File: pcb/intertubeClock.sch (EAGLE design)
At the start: 89 parts, among them Q1 BSA223SP, Q10 BSA223SP, Q11 BSA223SP, Q12 BSA223SP, Q13 BSA223SP, Q14 BSA223SP, Q15 BSA223SP, Q16 BSA223SP, Q2 BSA223SP, Q3 BSA223SP, Q4 BSA223SP, Q5 BSA223SP, Q6 BSA223SP, Q7 BSA223SP, Q8 BSA223SP, Q9 BSA223SP, U1 HV5122PG, U2 HV5122PG

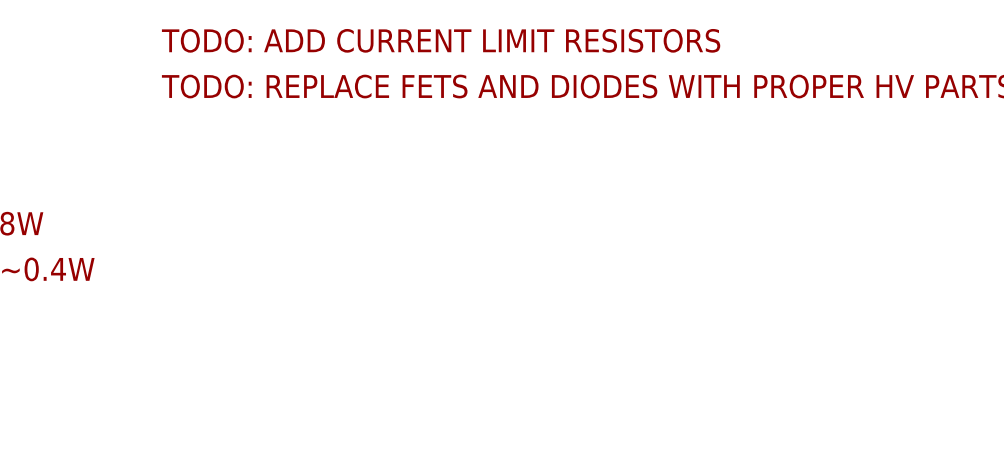
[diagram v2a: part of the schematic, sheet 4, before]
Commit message: -Fixed voltage divider values. -Added diodes.
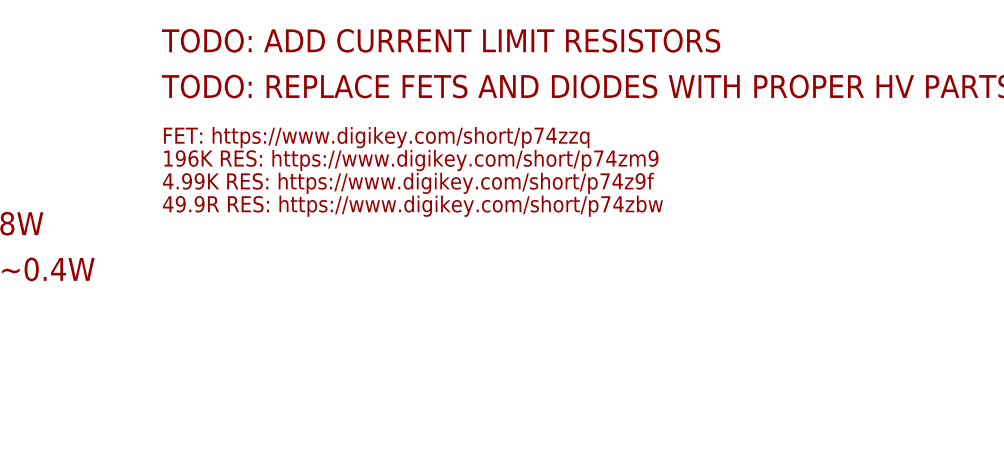
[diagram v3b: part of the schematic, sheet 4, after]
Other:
- note added: "196K RES: https://www.digikey.com/short/p74zm9"
- note added: "4.99K RES: https://www.digikey.com/short/p74z9f"
- note added: "49.9R RES: https://www.digikey.com/short/p74zbw"
- note added: "FET: https://www.digikey.com/short/p74zzq"
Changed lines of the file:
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@@
 <grid distance="0.1" unitdist="inch" unit="inch" style="lines" multiple="1" display="no" altdistance="0.01" altunitdist="inch" altunit="inch"/>
 <layers>
-<layer number="1" name="Top" color="4" fill="1" visible="yes" active="no"/>
-<layer number="2" name="Route2" color="1" fill="3" visible="yes" active="no"/>
-<layer number="3" name="Route3" color="4" fill="3" visible="yes" active="no"/>
-<layer number="4" name="Route4" color="1" fill="4" visible="yes" active="no"/>
-<layer number="5" name="Route5" color="4" fill="4" visible="yes" active="no"/>
-<layer number="6" name="Route6" color="1" fill="8" visible="yes" active="no"/>
-<layer number="7" name="Route7" color="4" fill="8" visible="yes" active="no"/>
-<layer number="8" name="Route8" color="1" fill="2" visible="yes" active="no"/>
-<layer number="9" name="Route9" color="4" fill="2" visible="yes" active="no"/>
-<layer number="10" name="Route10" color="1" fill="7" visible="yes" active="no"/>
-<layer number="11" name="Route11" color="4" fill="7" visible="yes" active="no"/>
-<layer number="12" name="Route12" color="1" fill="5" visible="yes" active="no"/>
-<layer number="13" name="Route13" color="4" fill="5" visible="yes" active="no"/>
-<layer number="14" name="Route14" color="1" fill="6" visible="yes" active="no"/>
-<layer number="15" name="Route15" color="4" fill="6" visible="yes" active="no"/>
-<layer number="16" name="Bottom" color="1" fill="1" visible="yes" active="no"/>
-<layer number="17" name="Pads" color="2" fill="1" visible="yes" active="no"/>
-<layer number="18" name="Vias" color="2" fill="1" visible="yes" active="no"/>
-<layer number="19" name="Unrouted" color="6" fill="1" visible="yes" active="no"/>
-<layer number="20" name="Dimension" color="15" fill="1" visible="yes" active="no"/>
-<layer number="21" name="tPlace" color="7" fill="1" visible="yes" active="no"/>
-<layer number="22" name="bPlace" color="7" fill="1" visible="yes" active="no"/>
-<layer number="23" name="tOrigins" color="15" fill="1" visible="yes" active="no"/>
-<layer number="24" name="bOrigins" color="15" fill="1" visible="yes" active="no"/>
-<layer number="25" name="tNames" color="7" fill="1" visible="yes" active="no"/>
-<layer number="26" name="bNames" color="7" fill="1" visible="yes" active="no"/>
-<layer number="27" name="tValues" color="7" fill="1" visible="yes" active="no"/>
-<layer number="28" name="bValues" color="7" fill="1" visible="yes" active="no"/>
+<layer number="1" name="Top" color="4" fill="1" visible="no" active="no"/>
+<layer number="2" name="Route2" color="1" fill="3" visible="no" active="no"/>
+<layer number="3" name="Route3" color="4" fill="3" visible="no" active="no"/>
+<layer number="4" name="Route4" color="1" fill="4" visible="no" active="no"/>
+<layer number="5" name="Route5" color="4" fill="4" visible="no" active="no"/>
+<layer number="6" name="Route6" color="1" fill="8" visible="no" active="no"/>
+<layer number="7" name="Route7" color="4" fill="8" visible="no" active="no"/>
+<layer number="8" name="Route8" color="1" fill="2" visible="no" active="no"/>
+<layer number="9" name="Route9" color="4" fill="2" visible="no" active="no"/>
+<layer number="10" name="Route10" color="1" fill="7" visible="no" active="no"/>
+<layer number="11" name="Route11" color="4" fill="7" visible="no" active="no"/>
+<layer number="12" name="Route12" color="1" fill="5" visible="no" active="no"/>
+<layer number="13" name="Route13" color="4" fill="5" visible="no" active="no"/>
+<layer number="14" name="Route14" color="1" fill="6" visible="no" active="no"/>
+<layer number="15" name="Route15" color="4" fill="6" visible="no" active="no"/>
+<layer number="16" name="Bottom" color="1" fill="1" visible="no" active="no"/>
+<layer number="17" name="Pads" color="2" fill="1" visible="no" active="no"/>
+<layer number="18" name="Vias" color="2" fill="1" visible="no" active="no"/>
+<layer number="19" name="Unrouted" color="6" fill="1" visible="no" active="no"/>
+<layer number="20" name="Dimension" color="15" fill="1" visible="no" active="no"/>
+<layer number="21" name="tPlace" color="7" fill="1" visible="no" active="no"/>
+<layer number="22" name="bPlace" color="7" fill="1" visible="no" active="no"/>
+<layer number="23" name="tOrigins" color="15" fill="1" visible="no" active="no"/>
+<layer number="24" name="bOrigins" color="15" fill="1" visible="no" active="no"/>
+<layer number="25" name="tNames" color="7" fill="1" visible="no" active="no"/>
+<layer number="26" name="bNames" color="7" fill="1" visible="no" active="no"/>
+<layer number="27" name="tValues" color="7" fill="1" visible="no" active="no"/>
+<layer number="28" name="bValues" color="7" fill="1" visible="no" active="no"/>
 <layer number="29" name="tStop" color="7" fill="3" visible="no" active="no"/>
 <layer number="30" name="bStop" color="7" fill="6" visible="no" active="no"/>
@@
 <layer number="35" name="tGlue" color="7" fill="4" visible="no" active="no"/>
 <layer number="36" name="bGlue" color="7" fill="5" visible="no" active="no"/>
-<layer number="37" name="tTest" color="7" fill="1" visible="yes" active="no"/>
-<layer number="38" name="bTest" color="7" fill="1" visible="yes" active="no"/>
+<layer number="37" name="tTest" color="7" fill="1" visible="no" active="no"/>
+<layer number="38" name="bTest" color="7" fill="1" visible="no" active="no"/>
 <layer number="39" name="tKeepout" color="4" fill="11" visible="no" active="no"/>
 <layer number="40" name="bKeepout" color="1" fill="11" visible="no" active="no"/>
@@
 <layer number="44" name="Drills" color="7" fill="1" visible="no" active="no"/>
 <layer number="45" name="Holes" color="7" fill="1" visible="no" active="no"/>
-<layer number="46" name="Milling" color="3" fill="1" visible="yes" active="no"/>
-<layer number="47" name="Measures" color="7" fill="1" visible="yes" active="no"/>
-<layer number="48" name="Document" color="7" fill="1" visible="yes" active="no"/>
-<layer number="49" name="Reference" color="7" fill="1" visible="yes" active="no"/>
-<layer number="51" name="tDocu" color="7" fill="1" visible="yes" active="no"/>
-<layer number="52" name="bDocu" color="7" fill="1" visible="yes" active="no"/>
+<layer number="46" name="Milling" color="3" fill="1" visible="no" active="no"/>
+<layer number="47" name="Measures" color="7" fill="1" visible="no" active="no"/>
+<layer number="48" name="Document" color="7" fill="1" visible="no" active="no"/>
+<layer number="49" name="Reference" color="7" fill="1" visible="no" active="no"/>
+<layer number="51" name="tDocu" color="7" fill="1" visible="no" active="no"/>
+<layer number="52" name="bDocu" color="7" fill="1" visible="no" active="no"/>
 <layer number="90" name="Modules" color="5" fill="1" visible="yes" active="yes"/>
 <layer number="91" name="Nets" color="2" fill="1" visible="yes" active="yes"/>
@@
 <text x="27.94" y="238.76" size="2.54" layer="94">Vba limiter dissipation = ~0.8W</text>
 <text x="27.94" y="233.68" size="2.54" layer="94">Vba_off limiter dissipation = ~0.4W</text>
+<text x="91.44" y="248.92" size="1.778" layer="94">FET: https://www.digikey.com/short/p74zzq</text>
+<text x="91.44" y="246.38" size="1.778" layer="94">196K RES: https://www.digikey.com/short/p74zm9</text>
+<text x="91.44" y="243.84" size="1.778" layer="94">4.99K RES: https://www.digikey.com/short/p74z9f</text>
+<text x="91.44" y="241.3" size="1.778" layer="94">49.9R RES: https://www.digikey.com/short/p74zbw</text>
 </plain>
 <instances>

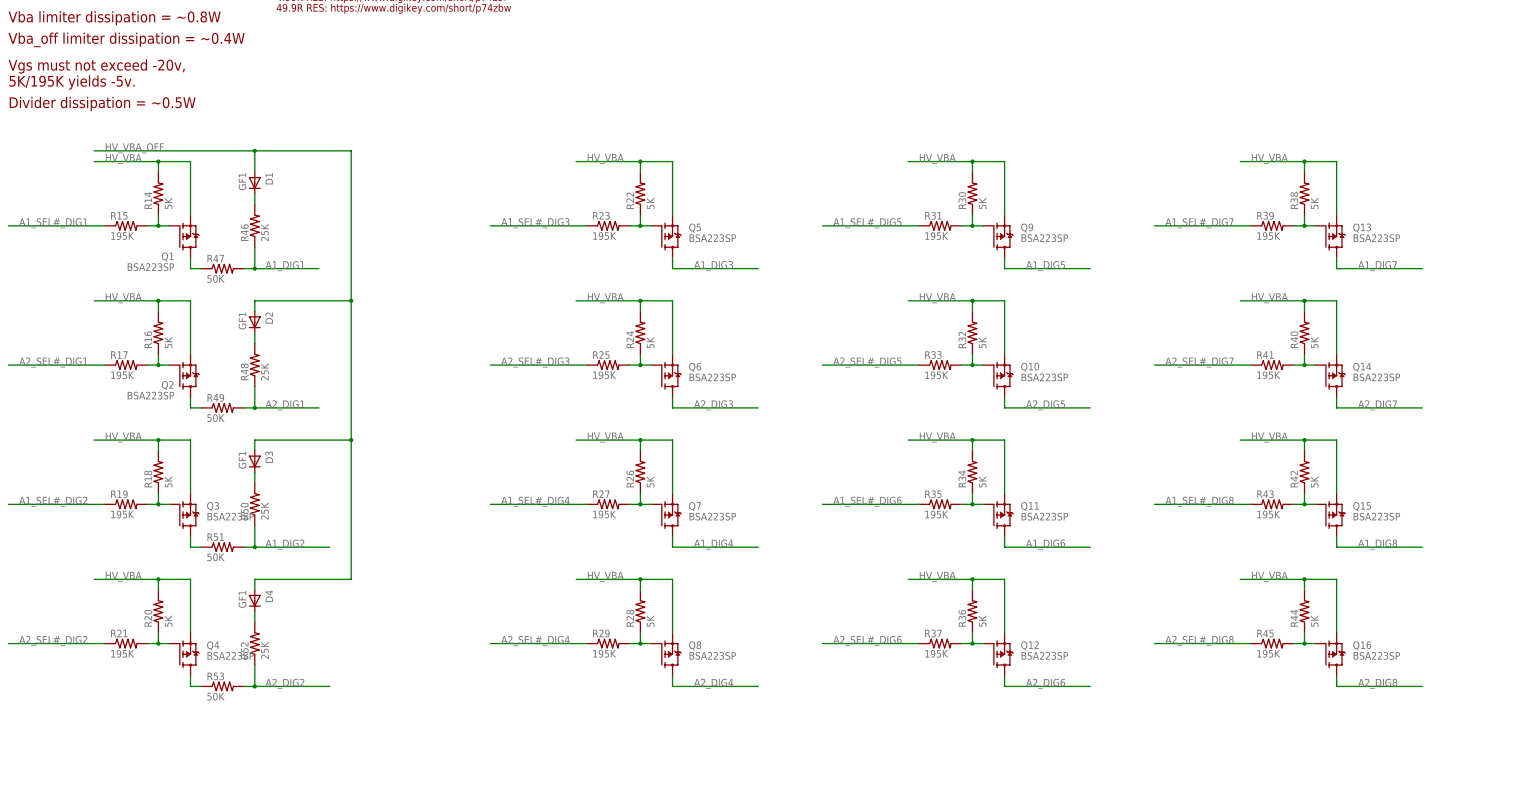
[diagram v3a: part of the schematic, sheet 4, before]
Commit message: -Added remaining components.
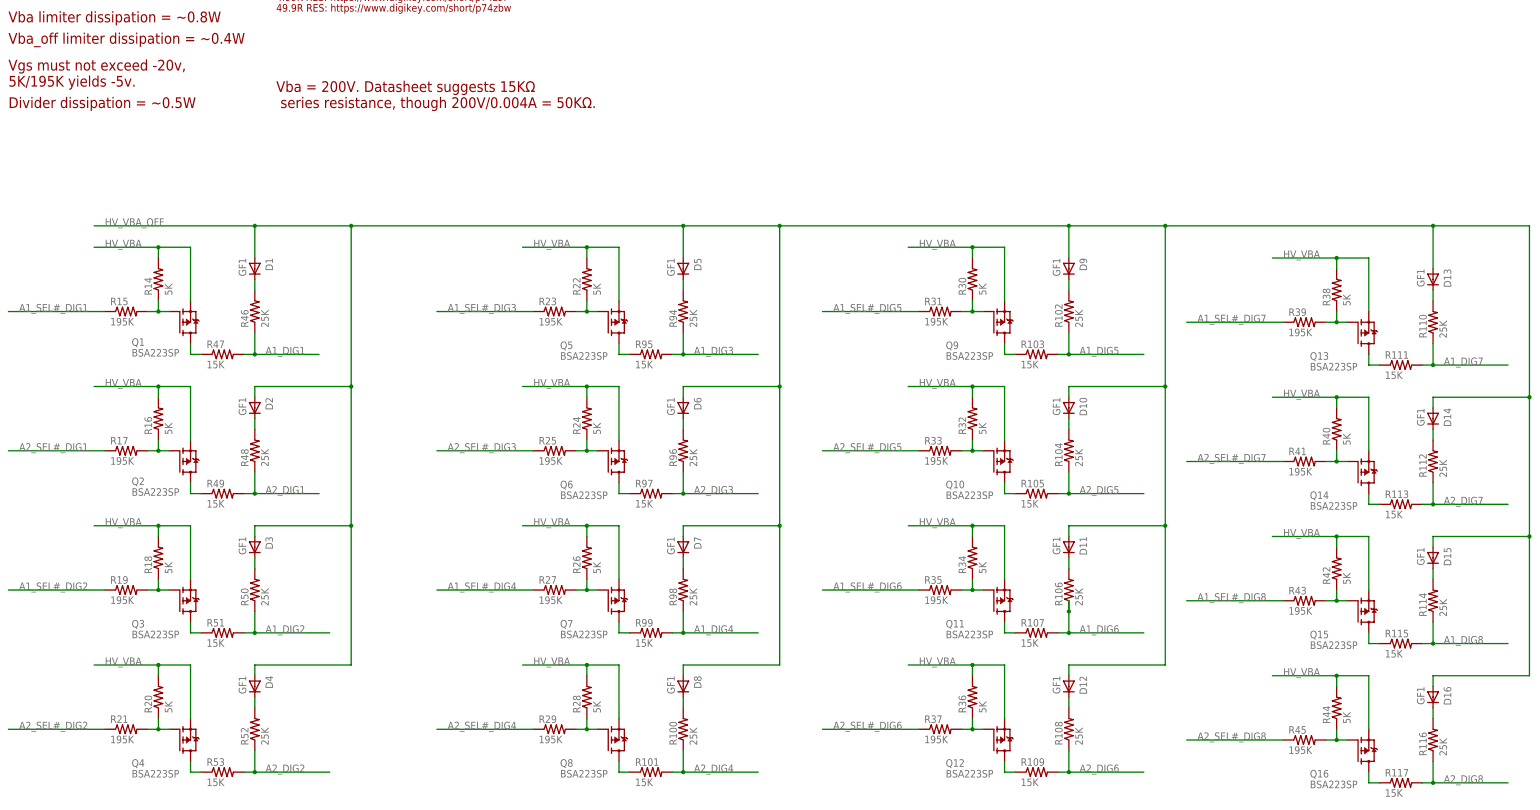
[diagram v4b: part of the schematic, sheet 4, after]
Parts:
- added D10, D11, D12, D13, D14, D15, D16, D5, D6, D7, D8, D9: GF1, diode:GF1
- added R100, R102, R104, R106, R108, R110, R112, R114, R116, R94, R96, R98: 25K, rcl:R-US_R1206
- added R101, R103, R105, R107, R109, R111, R113, R115, R117, R95, R97, R99: 15K, rcl:R-US_R1206
- added R54, R55, R56, R57, R58, R59, R60, R61, R62, R63, R64, R65, R66, R67, R68, R69, R70, R71, R72, R73, R74, R75, R76, R77, R78, R79, R80, R81, R82, R83, R84, R85, R86, R87, R88, R89, R90, R91, R92, R93: 100K, rcl:R-US_R1206
- R10, R11, R12, R13, R22, R23, R24, R25, R26, R27, R28, R29, R30, R31, R32, R33, R34, R35, R36, R37, R38, R39, R40, R41, R42, R43, R44, R45, R6, R7, R8, R9: device rcl:R-US_R2512 -> rcl:R-US_R1206
- R47, R49, R51, R53: value 50K -> 15K; device rcl:R-US_R2010 -> rcl:R-US_R1206
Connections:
- new net N$26: D5.C, R94.2
- new net N$27: D6.C, R96.2
- new net N$28: D7.C, R98.2
- new net N$29: D8.C, R100.2
- new net N$30: Q9.D, R103.1
- new net N$31: D9.C, R102.2
- new net N$32: D10.C, R104.2
- new net N$33: D11.C, R106.2
- new net N$34: D12.C, R108.2
- new net N$35: Q13.D, R111.1
- new net N$36: D13.C, R110.2
- new net N$37: D14.C, R112.2
- new net N$38: D15.C, R114.2
- new net N$39: D16.C, R116.2
- new net N$41: Q5.D, R95.1
- new net N$42: Q6.D, R97.1
- new net N$43: Q7.D, R99.1
- new net N$44: Q8.D, R101.1
- new net N$45: Q10.D, R105.1
- new net N$46: Q11.D, R107.1
- new net N$47: Q12.D, R109.1
- new net N$48: Q14.D, R113.1
- new net N$49: Q15.D, R115.1
- new net N$50: Q16.D, R117.1
- net A1_DIG3: now also R94.1, R95.2; no longer Q5.D
- net A1_DIG4: now also R98.1, R99.2; no longer Q7.D
- net A1_DIG5: now also R102.1, R103.2; no longer Q9.D
- net A1_DIG6: now also R106.1, R107.2; no longer Q11.D
- net A1_DIG7: now also R110.1, R111.2; no longer Q13.D
- net A1_DIG8: now also R114.1, R115.2; no longer Q15.D
- net A2_DIG3: now also R96.1, R97.2; no longer Q6.D
- net A2_DIG4: now also R100.1, R101.2; no longer Q8.D
- net A2_DIG5: now also R104.1, R105.2; no longer Q10.D
- net A2_DIG6: now also R108.1, R109.2; no longer Q12.D
- net A2_DIG7: now also R112.1, R113.2; no longer Q14.D
- net A2_DIG8: now also R116.1, R117.2; no longer Q16.D
- net HV_VBA_OFF: now also D10.A, D11.A, D12.A, D13.A, D14.A, D15.A, D16.A, D5.A, D6.A, D7.A, D8.A, D9.A
- net HV_VS: now also R54.1, R55.1, R56.1, R57.1, R58.1, R59.1, R60.1, R61.1, R62.1, R63.1, R64.1, R65.1, R66.1, R67.1, R68.1, R69.1, R70.1, R71.1, R72.1, R73.1, R74.1, R75.1, R76.1, R77.1, R78.1, R79.1, R80.1, R81.1, R82.1, R83.1, R84.1, R85.1, R86.1, R87.1, R88.1, R89.1, R90.1, R91.1, R92.1, R93.1
- net K01_DIG1: now also R54.2
- net K01_DIG2: now also R59.2
- net K01_DIG3: now also R64.2
- net K01_DIG4: now also R69.2
- net K01_DIG5: now also R74.2
- net K01_DIG6: now also R79.2
- net K01_DIG7: now also R84.2
- net K01_DIG8: now also R89.2
- net K23_DIG1: now also R55.2
- net K23_DIG2: now also R60.2
- net K23_DIG3: now also R65.2
- net K23_DIG4: now also R70.2
- net K23_DIG5: now also R75.2
- net K23_DIG6: now also R80.2
- net K23_DIG7: now also R85.2
- net K23_DIG8: now also R90.2
- net K45_DIG1: now also R56.2
- net K45_DIG2: now also R61.2
- net K45_DIG3: now also R66.2
- net K45_DIG4: now also R71.2
- net K45_DIG5: now also R76.2
- net K45_DIG6: now also R81.2
- net K45_DIG7: now also R86.2
- net K45_DIG8: now also R91.2
- net K67_DIG1: now also R57.2
- net K67_DIG2: now also R62.2
- net K67_DIG3: now also R67.2
- net K67_DIG4: now also R72.2
- net K67_DIG5: now also R77.2
- net K67_DIG6: now also R82.2
- net K67_DIG7: now also R87.2
- net K67_DIG8: now also R92.2
- net K89_DIG1: now also R58.2
- net K89_DIG2: now also R63.2
- net K89_DIG3: now also R68.2
- net K89_DIG4: now also R73.2
- net K89_DIG5: now also R78.2
- net K89_DIG6: now also R83.2
- net K89_DIG7: now also R88.2
- net K89_DIG8: now also R93.2
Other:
- note added: "2019.05.03"
- note added: "ADJUSTED RES VALUES. ADDED CATHODE PULLUPS. ADDED REMAINING COMPONENTS."
- note added: "Vba = 200V. Datasheet suggests 15KΩ series resistance, though 200V/0.004A = 50KΩ."
- note added: "Vs set to 50V."
- moved on the sheet: D1, D2, D3, D4, JP1, JP2, JP3, JP4, JP5, JP6, JP7, JP8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
